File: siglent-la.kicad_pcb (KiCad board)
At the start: 4 copper layers, 21.5 x 17.5 mm, 65 parts, among them J1 Bus_PCI_Express_x1

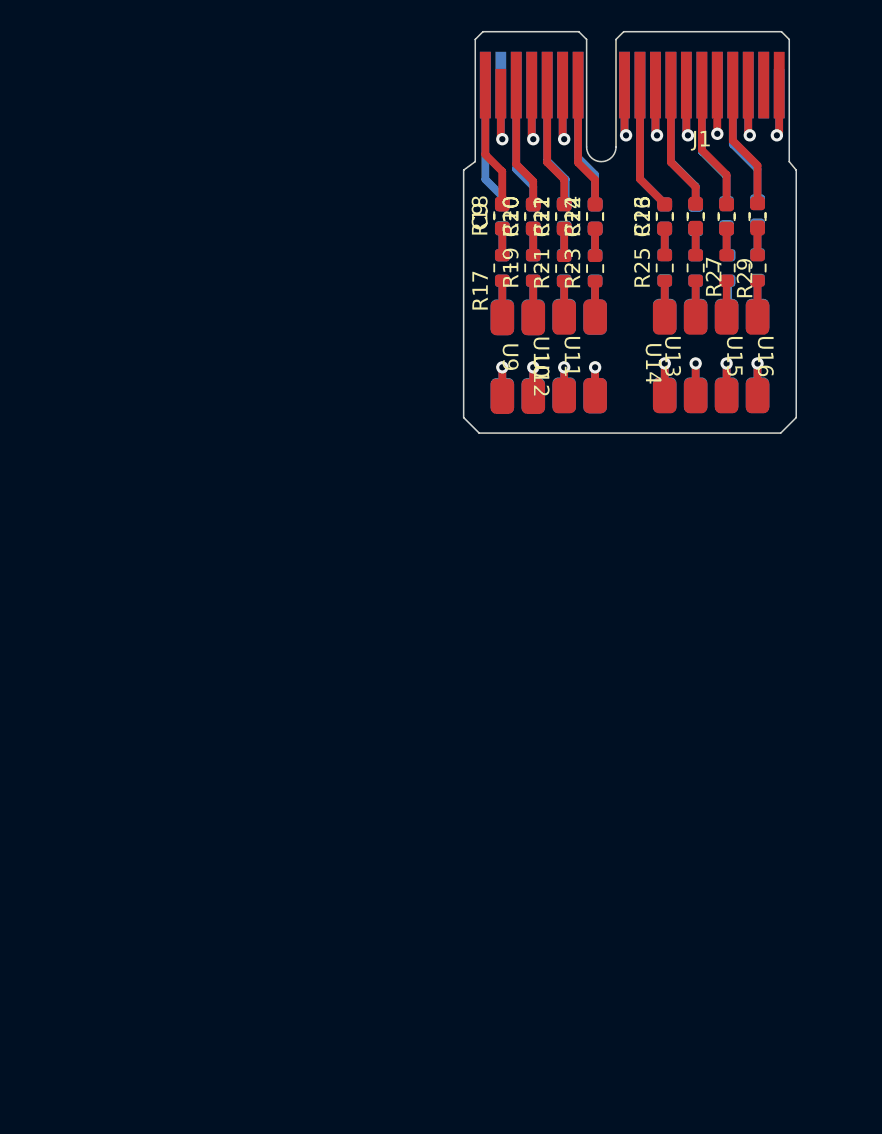
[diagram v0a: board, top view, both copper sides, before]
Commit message: rj45 version of the logic analyzer
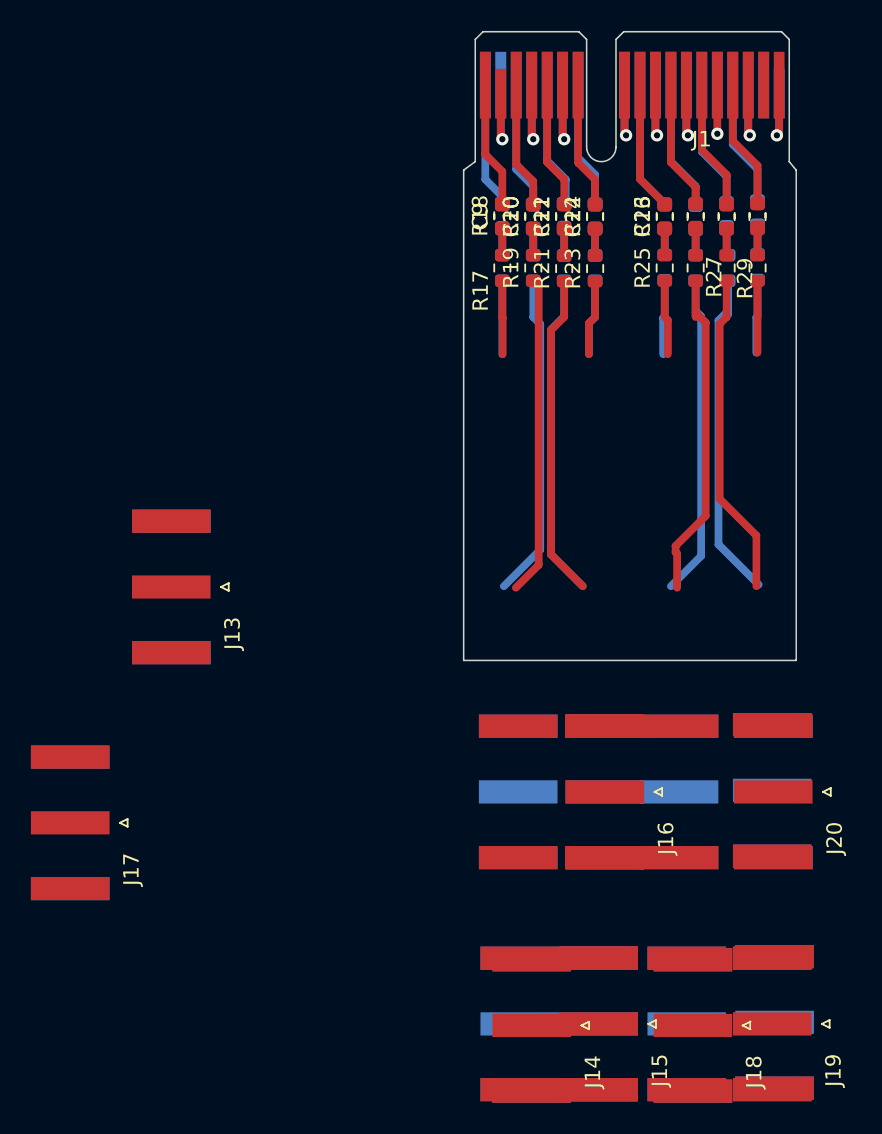
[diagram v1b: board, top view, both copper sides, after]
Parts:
- removed U1, U10, U11, U12, U13, U14, U15, U16, U2, U3, U4, U5, U6, U7, U8, U9: ~, solder_coax:solder_coax
- added J10: IPEX-004, Connector_Coaxial:SMA_Amphenol_132289_EdgeMount, B.Cu at (120.1, 127.6)
- added J12: IPEX-004, Connector_Coaxial:SMA_Amphenol_132289_EdgeMount, B.Cu at (120.0, 112.6)
- added J13: IPEX-004, Connector_Coaxial:SMA_Amphenol_132289_EdgeMount, F.Cu at (81.1, 99.5)
- added J14: IPEX-004, Connector_Coaxial:SMA_Amphenol_132289_EdgeMount, F.Cu at (104.4, 127.8)
- added J15: IPEX-004, Connector_Coaxial:SMA_Amphenol_132289_EdgeMount, F.Cu at (108.7, 127.7)
- added J16: IPEX-004, Connector_Coaxial:SMA_Amphenol_132289_EdgeMount, F.Cu at (109.1, 112.7)
- added J17: IPEX-004, Connector_Coaxial:SMA_Amphenol_132289_EdgeMount, F.Cu at (74.6, 114.7)
- added J18: IPEX-004, Connector_Coaxial:SMA_Amphenol_132289_EdgeMount, F.Cu at (114.8, 127.8)
- added J19: IPEX-004, Connector_Coaxial:SMA_Amphenol_132289_EdgeMount, F.Cu at (120.0, 127.7)
- added J2: IPEX-004, Connector_Coaxial:SMA_Amphenol_132289_EdgeMount, B.Cu at (103.5, 112.7)
- added J20: IPEX-004, Connector_Coaxial:SMA_Amphenol_132289_EdgeMount, F.Cu at (120.0, 112.7)
- added J3: IPEX-004, Connector_Coaxial:SMA_Amphenol_132289_EdgeMount, B.Cu at (103.6, 127.7)
- added J6: IPEX-004, Connector_Coaxial:SMA_Amphenol_132289_EdgeMount, B.Cu at (108.7, 127.7)
- added J7: IPEX-004, Connector_Coaxial:SMA_Amphenol_132289_EdgeMount, B.Cu at (109.1, 112.7)
- added J8: IPEX-004, Connector_Coaxial:SMA_Amphenol_132289_EdgeMount, B.Cu at (113.9, 112.7)
- added J9: IPEX-004, Connector_Coaxial:SMA_Amphenol_132289_EdgeMount, B.Cu at (114.4, 127.7)
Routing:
- net GND: track 87.6 -> 56.4 mm, vias 17 -> 9
- net Net-(J18-In): track 2.35 -> 21.3 mm
- net Net-(J10-In): track 2.35 -> 21.2 mm
- net Net-(J9-In): track 2.31 -> 21.1 mm
- net Net-(J6-In): track 2.31 -> 21.0 mm
- net Net-(J15-In): track 2.31 -> 20.9 mm
- net Net-(J19-In): track 2.35 -> 20.9 mm
- net Net-(J3-In): track 2.35 -> 20.9 mm
- net Net-(J14-In): track 2.39 -> 20.6 mm
- net Net-(J7-In): track 2.35 -> 4.92 mm
- net Net-(J16-In): track 2.31 -> 4.88 mm
- net Net-(J17-In): track 2.35 -> 4.83 mm
- net Net-(J8-In): track 2.33 -> 4.82 mm
- net Net-(J2-In): track 2.35 -> 4.75 mm
- net Net-(J12-In): track 2.36 -> 4.73 mm
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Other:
- board size 21.5 x 17.5 mm -> 21.5 x 32.2 mm
